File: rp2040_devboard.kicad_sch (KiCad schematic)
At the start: 13 parts, among them U1 RP2040

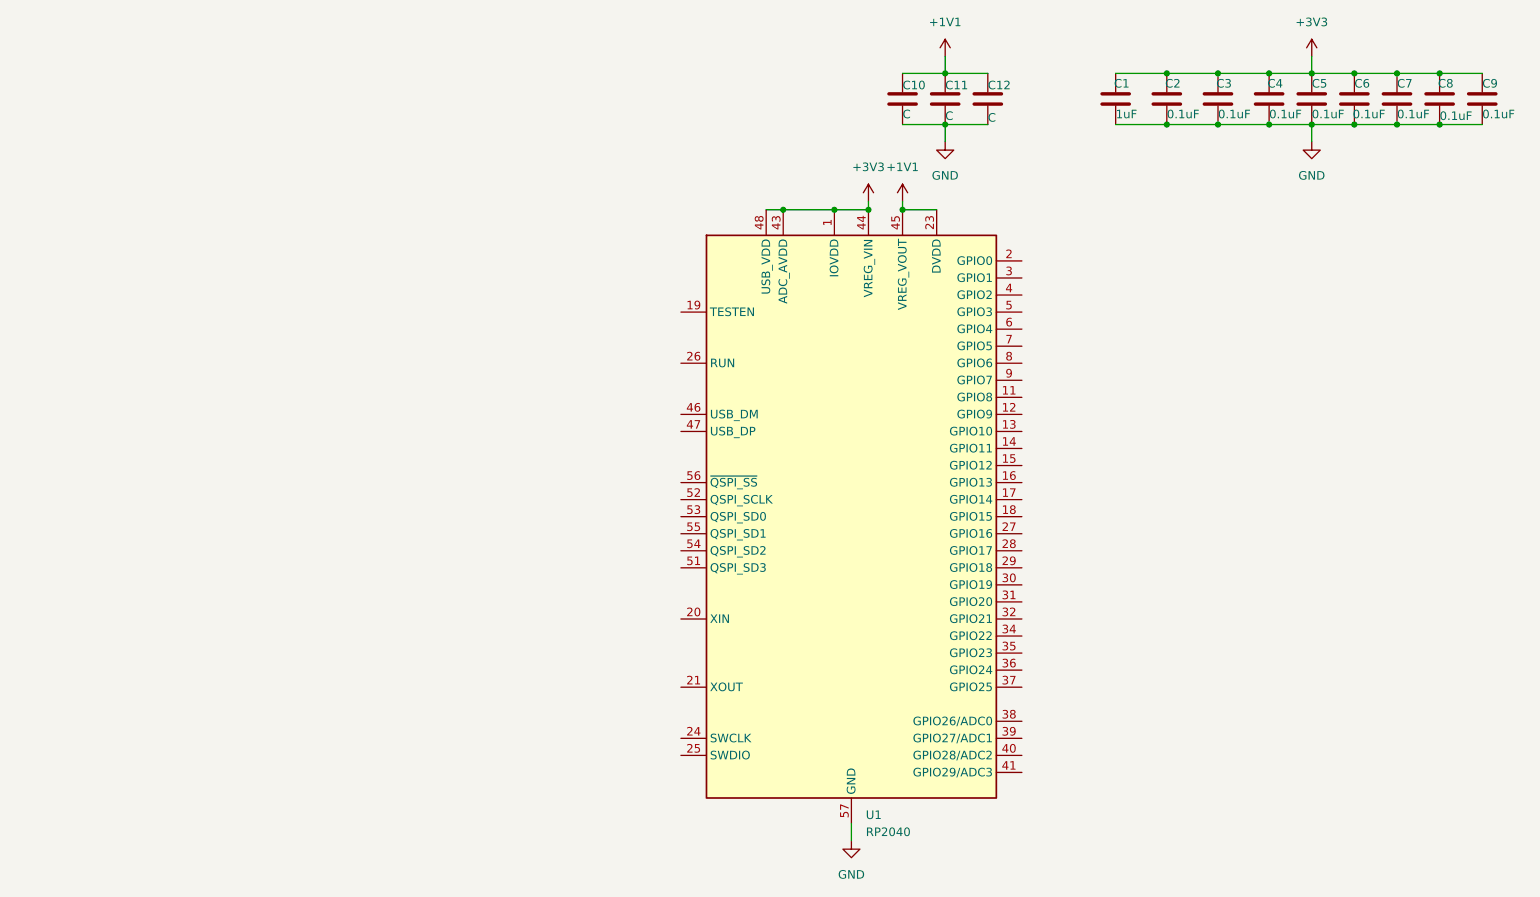
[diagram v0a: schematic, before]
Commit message: USB-C created and added couple of global labels
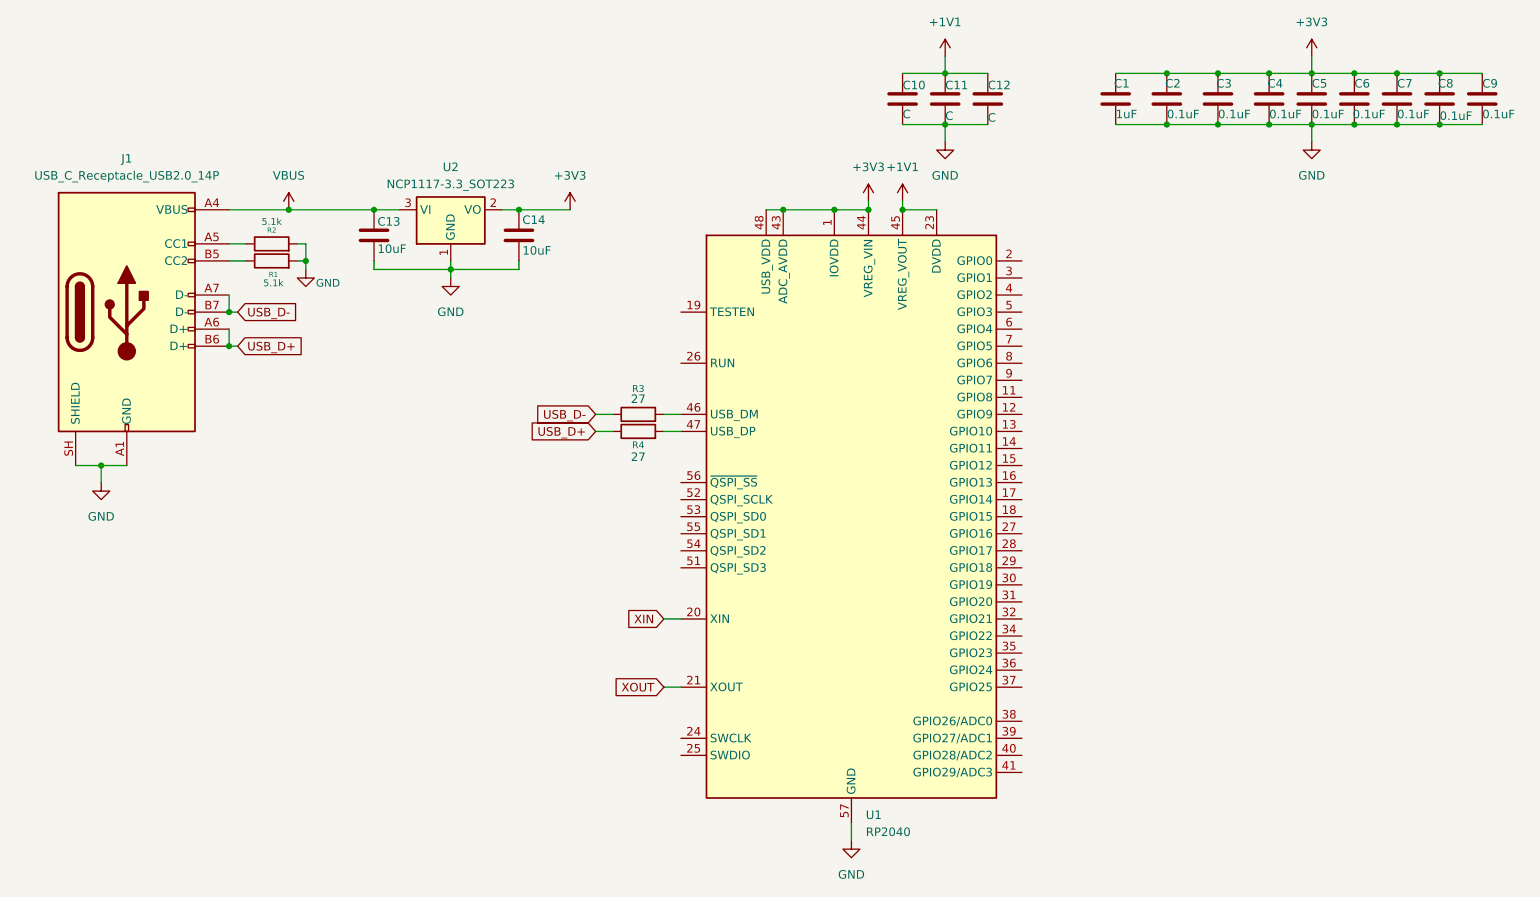
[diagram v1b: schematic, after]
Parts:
- added C13, C14: 10uF, symbol Device:C
- added J1: USB_C_Receptacle_USB2.0_14P, symbol Connector:USB_C_Receptacle_USB2.0_14P
- added R1, R2: 5.1k, symbol Device:R
- added R3, R4: 27, symbol Device:R
- added U2: NCP1117-3.3_SOT223, Package_TO_SOT_SMD:SOT-223-3_TabPin2, symbol Regulator_Linear:NCP1117-3.3_SOT223
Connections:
- net +3V3: now also C14.1, U2.2 (VO)
- net GND: now also C13.2, C14.2, J1.A1 (GND), J1.A12 (GND), J1.B1 (GND), J1.B12 (GND), J1.SH (SHIELD), R1.2, R2.2, U2.1 (GND)
- net XIN: now reaches U1.20 (XIN)
- net XOUT: now reaches U1.21 (XOUT)
- net at U1.46 (USB_DM): now also R3.2
- net at U1.47 (USB_DP): now also R4.2
- new net: J1.A5 (CC1), R2.1
- new net: J1.B5 (CC2), R1.1
- new net USB_D+: J1.A6 (D+), J1.B6 (D+), R4.1
- new net USB_D-: J1.A7 (D-), J1.B7 (D-), R3.1
- new net VBUS: C13.1, J1.A4 (VBUS), J1.A9 (VBUS), J1.B4 (VBUS), J1.B9 (VBUS), U2.3 (VI)

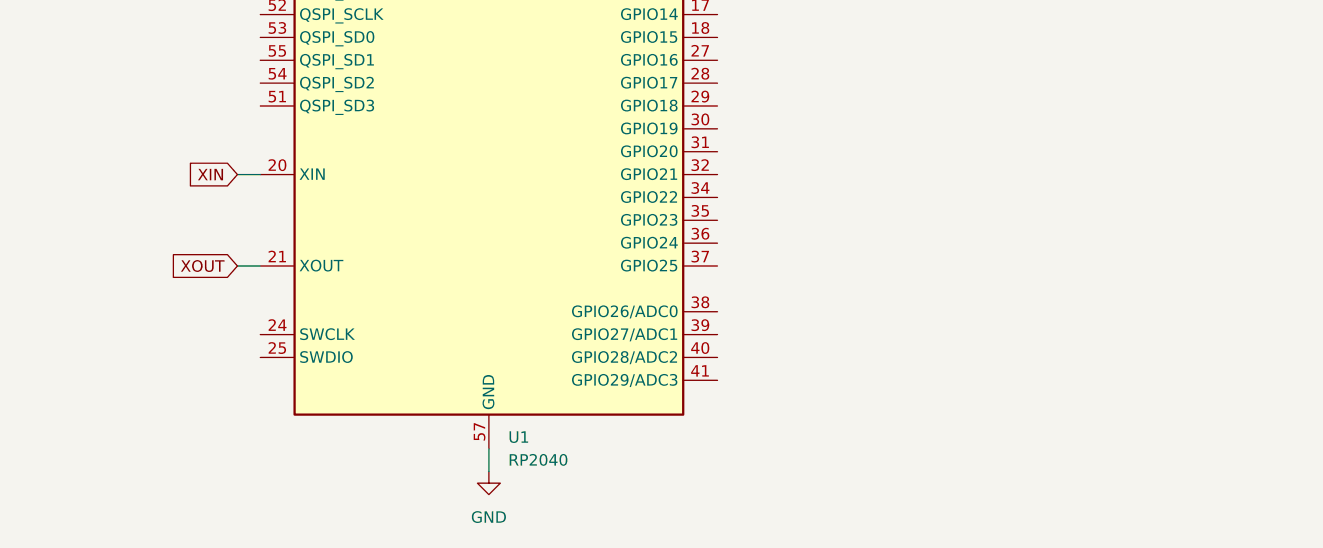
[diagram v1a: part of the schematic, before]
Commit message: Added crystal oscilator to the schematic
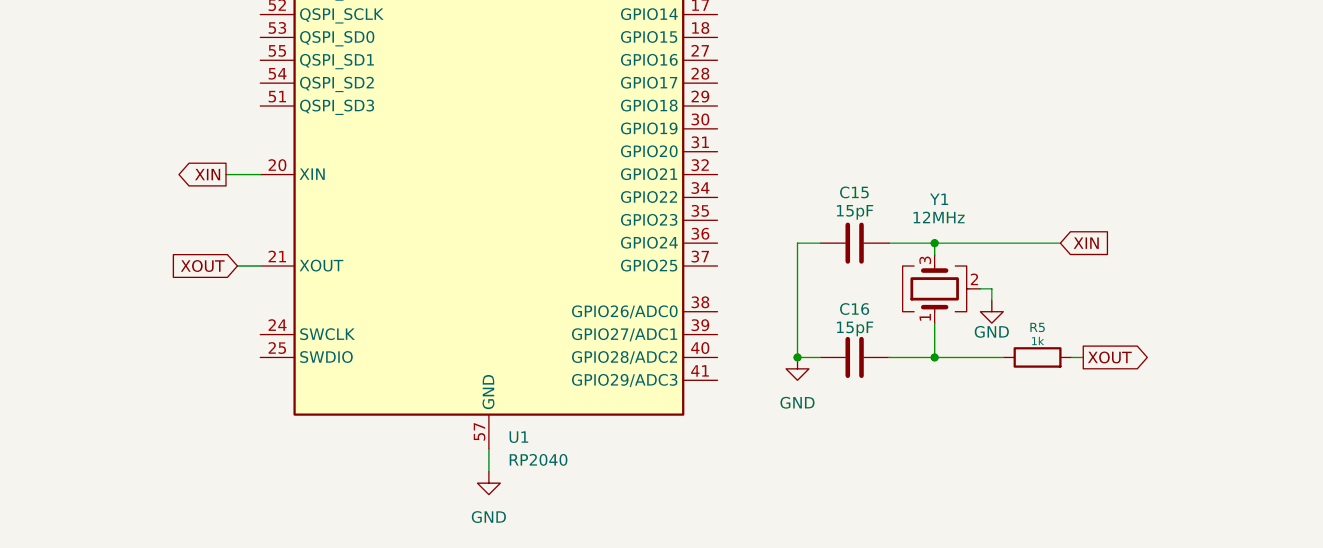
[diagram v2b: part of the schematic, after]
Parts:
- added C15, C16: 15pF, symbol Device:C
- added R5: 1k, symbol Device:R
- added Y1: 12MHz, symbol Device:Crystal_GND24
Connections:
- net GND: now also C15.1, C16.1, Y1.2 (G), Y1.4 (G)
- net XIN: now also C15.2, Y1.3
- net XOUT: now also R5.2
- new net: C16.2, R5.1, Y1.1
